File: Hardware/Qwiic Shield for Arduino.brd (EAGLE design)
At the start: 53.3 x 59.7 mm, 35 parts, among them Q1 200mA/50V, Q2 200mA/50V, U1 ARDUINO UNO

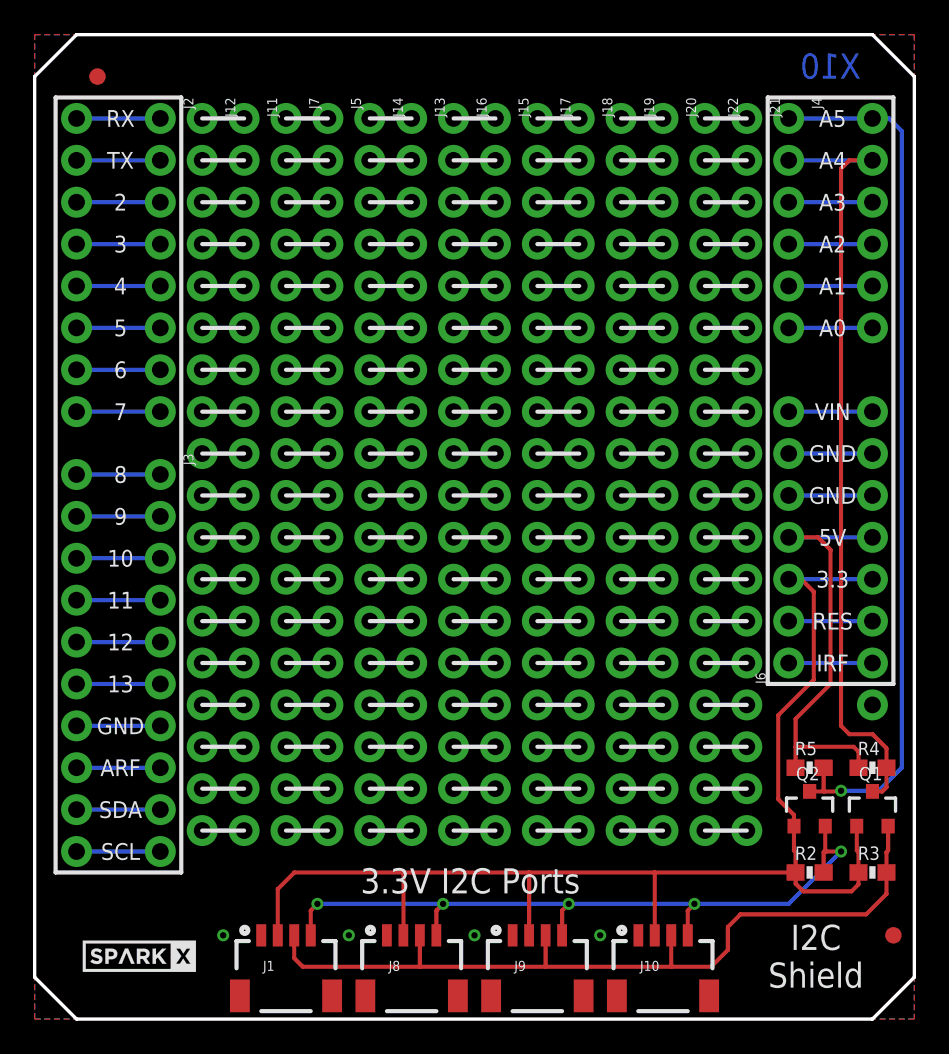
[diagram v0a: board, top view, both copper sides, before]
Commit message: Adding mounting spot for Qwiic boards
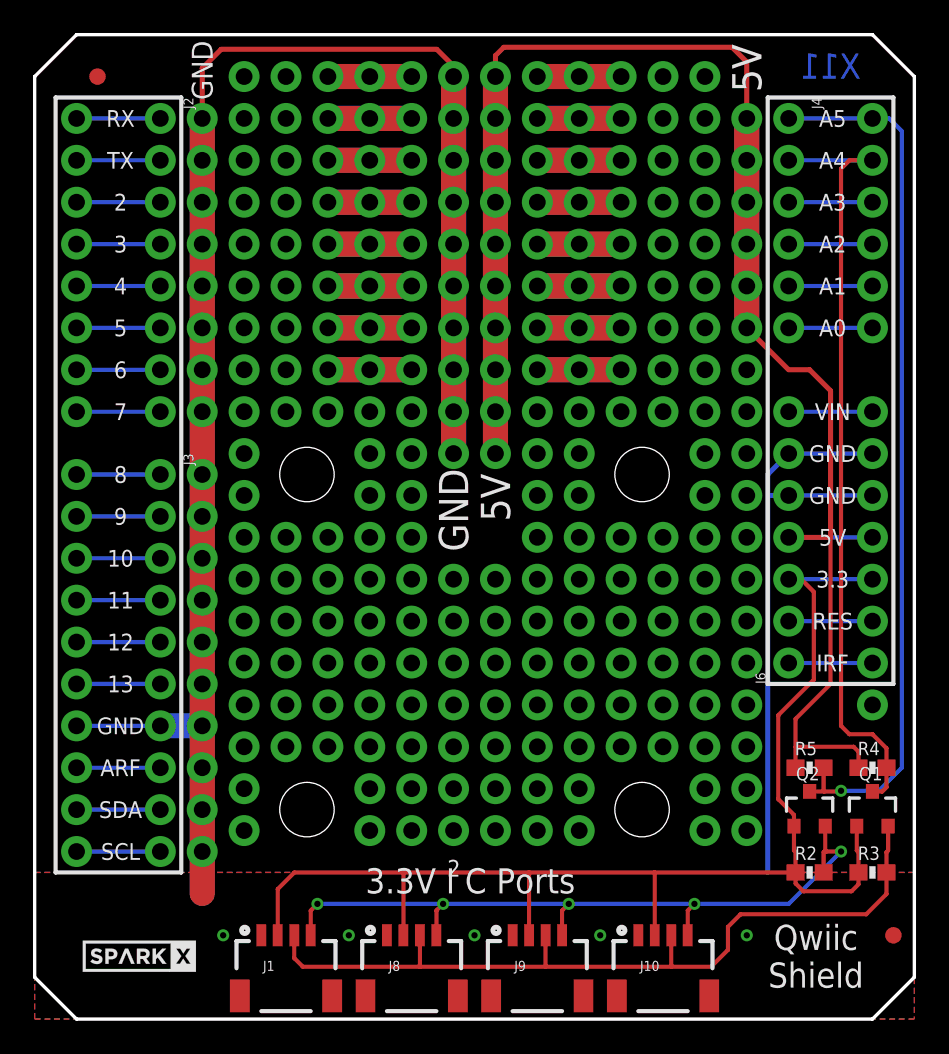
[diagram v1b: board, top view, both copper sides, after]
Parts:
- removed J11, J12, J13, J14, J15, J16, J17, J18, J19, J20, J21, J22, J5, J7: (no value), SparkX:1X18_NO_SILK
- added U$3: QWIIC_BOARD_OUTLINEH, SparkX:QWIIC_BOARD_MOUNT_HOLES
- moved LOGO1 3.81 mm to (47.0, 7.62)
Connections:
- removed net N$1: J5.2, J7.2
- removed net N$10: J5.11, J7.11
- removed net N$100: J19.11, J20.11
- removed net N$101: J19.12, J20.12
- removed net N$102: J19.13, J20.13
- removed net N$103: J19.14, J20.14
- removed net N$104: J19.15, J20.15
- removed net N$105: J19.16, J20.16
- removed net N$106: J19.17, J20.17
- removed net N$107: J19.18, J20.18
- removed net N$108: J19.1, J20.1
- removed net N$109: J21.2, J22.2
- removed net N$11: J5.12, J7.12
- removed net N$110: J21.3, J22.3
- removed net N$111: J21.4, J22.4
- removed net N$112: J21.5, J22.5
- removed net N$113: J21.6, J22.6
- removed net N$114: J21.7, J22.7
- removed net N$115: J21.8, J22.8
- removed net N$116: J21.9, J22.9
- removed net N$117: J21.10, J22.10
- removed net N$118: J21.11, J22.11
- removed net N$119: J21.12, J22.12
- removed net N$12: J5.13, J7.13
- removed net N$120: J21.13, J22.13
- removed net N$121: J21.14, J22.14
- removed net N$122: J21.15, J22.15
- removed net N$123: J21.16, J22.16
- removed net N$124: J21.17, J22.17
- removed net N$125: J21.18, J22.18
- removed net N$126: J21.1, J22.1
- removed net N$13: J5.14, J7.14
- removed net N$14: J5.15, J7.15
- removed net N$15: J5.16, J7.16
- removed net N$16: J5.17, J7.17
- removed net N$17: J5.18, J7.18
- removed net N$18: J5.1, J7.1
- removed net N$19: J13.2, J14.2
- removed net N$2: J5.3, J7.3
- removed net N$20: J13.3, J14.3
- removed net N$21: J11.2, J12.2
- removed net N$22: J11.3, J12.3
- removed net N$23: J11.4, J12.4
- removed net N$24: J11.5, J12.5
- removed net N$25: J11.6, J12.6
- removed net N$26: J11.7, J12.7
- removed net N$27: J11.8, J12.8
- removed net N$28: J11.9, J12.9
- removed net N$29: J11.10, J12.10
- removed net N$3: J5.4, J7.4
- removed net N$30: J11.11, J12.11
- removed net N$31: J11.12, J12.12
- removed net N$32: J11.13, J12.13
- removed net N$33: J11.14, J12.14
- removed net N$34: J11.15, J12.15
- removed net N$35: J11.16, J12.16
- removed net N$36: J11.17, J12.17
- removed net N$37: J11.18, J12.18
- removed net N$38: J11.1, J12.1
- removed net N$39: J13.4, J14.4
- removed net N$4: J5.5, J7.5
- removed net N$40: J13.5, J14.5
- removed net N$41: J13.6, J14.6
- removed net N$42: J13.7, J14.7
- removed net N$43: J13.8, J14.8
- removed net N$44: J13.9, J14.9
- removed net N$45: J13.10, J14.10
- removed net N$46: J13.11, J14.11
- removed net N$47: J13.12, J14.12
- removed net N$48: J13.13, J14.13
- removed net N$49: J13.14, J14.14
- removed net N$5: J5.6, J7.6
- removed net N$50: J13.15, J14.15
- removed net N$51: J13.16, J14.16
- removed net N$52: J13.17, J14.17
- removed net N$53: J13.18, J14.18
- removed net N$54: J13.1, J14.1
- removed net N$55: J15.2, J16.2
- removed net N$56: J15.3, J16.3
- removed net N$57: J15.4, J16.4
- removed net N$58: J15.5, J16.5
- removed net N$59: J15.6, J16.6
- removed net N$6: J5.7, J7.7
- removed net N$60: J15.7, J16.7
- removed net N$61: J15.8, J16.8
- removed net N$62: J15.9, J16.9
- removed net N$63: J15.10, J16.10
- removed net N$64: J15.11, J16.11
- removed net N$65: J15.12, J16.12
- removed net N$66: J15.13, J16.13
- removed net N$67: J15.14, J16.14
- removed net N$68: J15.15, J16.15
- removed net N$69: J15.16, J16.16
- removed net N$7: J5.8, J7.8
- removed net N$70: J15.17, J16.17
- removed net N$71: J15.18, J16.18
- removed net N$72: J15.1, J16.1
- removed net N$73: J17.2, J18.2
- removed net N$74: J17.3, J18.3
- removed net N$75: J17.4, J18.4
- removed net N$76: J17.5, J18.5
- removed net N$77: J17.6, J18.6
- removed net N$78: J17.7, J18.7
- removed net N$79: J17.8, J18.8
- removed net N$8: J5.9, J7.9
- removed net N$80: J17.9, J18.9
- removed net N$81: J17.10, J18.10
- removed net N$82: J17.11, J18.11
- removed net N$83: J17.12, J18.12
- removed net N$84: J17.13, J18.13
- removed net N$85: J17.14, J18.14
- removed net N$86: J17.15, J18.15
- removed net N$87: J17.16, J18.16
- removed net N$88: J17.17, J18.17
- removed net N$89: J17.18, J18.18
- removed net N$9: J5.10, J7.10
- removed net N$90: J17.1, J18.1
- removed net N$91: J19.2, J20.2
- removed net N$92: J19.3, J20.3
- removed net N$93: J19.4, J20.4
- removed net N$94: J19.5, J20.5
- removed net N$95: J19.6, J20.6
- removed net N$96: J19.7, J20.7
- removed net N$97: J19.8, J20.8
- removed net N$98: J19.9, J20.9
- removed net N$99: J19.10, J20.10
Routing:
- net GND: track 15.2 -> 205.1 mm, vias 4 -> 33
- net 5V: track 26.9 -> 134.6 mm, vias 0 -> 16
- net CH8: track 0.00 -> 10.2 mm, vias 0 -> 3
- net CH7: track 0.00 -> 10.2 mm, vias 0 -> 3
- net CH6: track 0.00 -> 10.2 mm, vias 0 -> 3
- net CH5: track 0.00 -> 10.2 mm, vias 0 -> 3
- net CH4: track 0.00 -> 10.2 mm, vias 0 -> 3
- net CH3: track 0.00 -> 10.2 mm, vias 0 -> 3
- net CH2: track 0.00 -> 10.2 mm, vias 0 -> 3
- net CH1: track 0.00 -> 10.2 mm, vias 0 -> 3
- net CH9: track 0.00 -> 10.2 mm, vias 0 -> 3
- net CH16: track 0.00 -> 10.2 mm, vias 0 -> 3
- net CH15: track 0.00 -> 10.2 mm, vias 0 -> 3
- net CH14: track 0.00 -> 10.2 mm, vias 0 -> 3
- net CH13: track 0.00 -> 10.2 mm, vias 0 -> 3
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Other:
- board text added: "3.3V I C Ports"
- board text added: "Qwiic Shield"
- board text added: "X11"
- board text removed: "3.3V I2C Ports"
- board text removed: "I2C Shield"
- board text removed: "X10"

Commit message: Adding panel
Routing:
- net CH8: track 10.2 -> 0.00 mm, vias 3 -> 0
- net CH16: track 10.2 -> 0.00 mm, vias 3 -> 0
- net 5V: track 134.6 -> 129.8 mm
- net GND: track 205.1 -> 201.4 mm

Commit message: Adding Qwiic mounting holes to shield
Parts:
- Q1, Q2: value 200mA/50V -> BSS138
